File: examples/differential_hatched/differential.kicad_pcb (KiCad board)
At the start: 2 copper layers, 2.1 x 3.6 mm, 4 parts

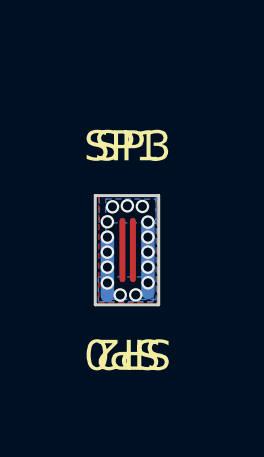
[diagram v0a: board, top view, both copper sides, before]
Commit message: Update examples with corrected settings and keep track of exported gerbers
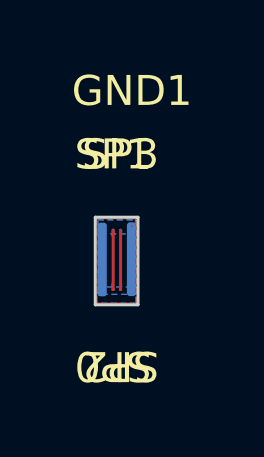
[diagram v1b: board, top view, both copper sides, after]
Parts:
- added GND1: Ground, simulation_port:pad_0.05mm, F.Cu at (149.2, 126.4)
- SP0, SP1, SP2, SP3: footprint custom:test_pad_0 -> simulation_port:pad_0.1mm
- moved SP2 0.58 mm to (148.8, 126.5)
- moved SP0 0.51 mm to (148.6, 126.5)
- moved SP3 0.49 mm to (148.8, 128.5)
- moved SP1 0.41 mm to (148.6, 128.5)
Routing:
- net GND: track 4.30 -> 0.00 mm, vias 15 -> 0
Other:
- board size 2.1 x 3.6 mm -> 1.4 x 2.9 mm
